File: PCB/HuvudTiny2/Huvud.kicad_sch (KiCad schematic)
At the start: 101 parts, among them J1 MOLEX Micro Fit 2x3, J2 DBG, J3 THERM, J4 FAN0, J5 FAN1, J6 Heater, J7 Endstop, J8 THERM, J9 STEPPER, Q1 AO3400A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

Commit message: Update screw terminal to molex connector.
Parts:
- J6: footprint Huvud:TerminalBlock_Phoenix_PT-1,5-2-3.5-H_1x02_P3.50mm_Horizontal -> Connector_Molex:Molex_Micro-Fit_3.0_43045-0200_2x01_P3.00mm_Horizontal
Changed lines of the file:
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@@
+    (pin "2")
+  )
+  (symbol (lib_id "Device:D") (at 194.945 109.22 0) (unit 1)
+    (in_bom yes) (on_board yes)
+    (property "Reference" "D4" (id 0) (at 191.77 108.3522 0))
+    (property "Value" "PMEG6010CEJ" (id 1) (at 194.945 105.5709 0))
+    (property "Footprint" "Diode_SMD:D_SOD-323F" (id 2) (at 194.945 109.22 0)
+      (effects (font (size 1.27 1.27)) hide)
+    )
+    (property "Datasheet" "~" (id 3) (at 194.945 109.22 0)
+      (effects (font (size 1.27 1.27)) hide)
+    )
+    (property "LCSC" "C406049" (id 4) (at 194.945 109.22 0)
+      (effects (font (size 1.27 1.27)) hide)
+    )
+    (pin "1")
     (pin "2")
   )
@@
     (pin "1")
   )
-  (symbol (lib_id "Device:D") (at 194.945 109.22 0) (unit 1)
-    (in_bom yes) (on_board yes)
-    (property "Reference" "D4" (id 0) (at 191.77 108.3522 0))
-    (property "Value" "PMEG6010CEJ" (id 1) (at 194.945 105.5709 0))
-    (property "Footprint" "Diode_SMD:D_SOD-323F" (id 2) (at 194.945 109.22 0)
-      (effects (font (size 1.27 1.27)) hide)
-    )
-    (property "Datasheet" "~" (id 3) (at 194.945 109.22 0)
-      (effects (font (size 1.27 1.27)) hide)
-    )
-    (property "LCSC" "C406049" (id 4) (at 194.945 109.22 0)
-      (effects (font (size 1.27 1.27)) hide)
-    )
-    (pin "1")
-    (pin "2")
-  )
   (symbol (lib_id "Mechanical:MountingHole_Pad") (at 249.555 118.745 0) (unit 1)
     (in_bom yes) (on_board yes)
@@
     (property "Reference" "J6" (id 0) (at 28.7528 168.91 0))
     (property "Value" "Heater" (id 1) (at 28.7528 170.4086 0))
-    (property "Footprint" "Huvud:TerminalBlock_Phoenix_PT-1,5-2-3.5-H_1x02_P3.50mm_Horizontal" (id 2) (at 29.21 172.72 0)
+    (property "Footprint" "Connector_Molex:Molex_Micro-Fit_3.0_43045-0200_2x01_P3.00mm_Horizontal" (id 2) (at 29.21 172.72 0)
       (effects (font (size 1.27 1.27)) hide)
     )
@@
     (pin "3")
     (pin "4")
+  )
+  (symbol (lib_id "Diode:BAT54S") (at 111.76 150.495 270) (mirror x) (unit 1)
+    (in_bom yes) (on_board yes)
+    (property "Reference" "D7" (id 0) (at 114.935 147.32 90))
+    (property "Value" "BAT54S" (id 1) (at 117.0686 145.415 90))
+    (property "Footprint" "Package_TO_SOT_SMD:SOT-23" (id 2) (at 114.935 148.59 0)
+      (effects (font (size 1.27 1.27)) (justify left) hide)
+    )
+    (property "Datasheet" "" (id 3) (at 111.76 153.543 0)
+      (effects (font (size 1.27 1.27)) hide)
+    )
+    (property "LCSC" "C12765" (id 4) (at 111.76 150.495 0)
+      (effects (font (size 1.27 1.27)) hide)
+    )
+    (pin "1")
+    (pin "2")
+    (pin "3")
+  )
+  (symbol (lib_id "Diode:BAT54S") (at 142.875 150.495 270) (mirror x) (unit 1)
+    (in_bom yes) (on_board yes)
+    (property "Reference" "D9" (id 0) (at 146.05 147.32 90))
+    (property "Value" "BAT54S" (id 1) (at 148.1836 145.415 90))
+    (property "Footprint" "Package_TO_SOT_SMD:SOT-23" (id 2) (at 146.05 148.59 0)
+      (effects (font (size 1.27 1.27)) (justify left) hide)
+    )
+    (property "Datasheet" "" (id 3) (at 142.875 153.543 0)
+      (effects (font (size 1.27 1.27)) hide)
+    )
+    (property "LCSC" "C12765" (id 4) (at 142.875 150.495 0)
+      (effects (font (size 1.27 1.27)) hide)
+    )
+    (pin "1")
+    (pin "2")
+    (pin "3")
+  )
+  (symbol (lib_id "Transistor_FET:2N7002") (at 50.8 121.92 0) (unit 1)
+    (in_bom yes) (on_board yes)
+    (property "Reference" "Q1" (id 0) (at 56.007 120.7516 0)
+      (effects (font (size 1.27 1.27)) (justify left))
+    )
+    (property "Value" "AO3400A" (id 1) (at 56.007 123.063 0)
+      (effects (font (size 1.27 1.27)) (justify left))
+    )
+    (property "Footprint" "Package_TO_SOT_SMD:SOT-23" (id 2) (at 55.88 123.825 0)
+      (effects (font (size 1.27 1.27) italic) (justify left) hide)
+    )
+    (property "Datasheet" "" (id 3) (at 50.8 121.92 0)
+      (effects (font (size 1.27 1.27)) (justify left) hide)
+    )
+    (property "LCSC" "C20917" (id 4) (at 50.8 121.92 0)
+      (effects (font (size 1.27 1.27)) hide)
+    )
+    (pin "1")
+    (pin "2")
+    (pin "3")
+  )
+  (symbol (lib_id "Transistor_FET:2N7002") (at 52.07 151.13 0) (unit 1)
+    (in_bom yes) (on_board yes)
+    (property "Reference" "Q2" (id 0) (at 57.277 149.9616 0)
+      (effects (font (size 1.27 1.27)) (justify left))
+    )
+    (property "Value" "AO3400A" (id 1) (at 57.277 152.273 0)
+      (effects (font (size 1.27 1.27)) (justify left))
+    )
+    (property "Footprint" "Package_TO_SOT_SMD:SOT-23" (id 2) (at 57.15 153.035 0)
+      (effects (font (size 1.27 1.27) italic) (justify left) hide)
+    )
+    (property "Datasheet" "" (id 3) (at 52.07 151.13 0)
+      (effects (font (size 1.27 1.27)) (justify left) hide)
+    )
+    (property "LCSC" "C20917" (id 4) (at 52.07 151.13 0)
+      (effects (font (size 1.27 1.27)) hide)
+    )
+    (pin "1")
+    (pin "2")
+    (pin "3")
+  )
+  (symbol (lib_id "Huvud:AON7418") (at 54.61 167.64 0) (unit 1)
+    (in_bom yes) (on_board yes)
+    (property "Reference" "Q3" (id 0) (at 57.15 179.07 0)
+      (effects (font (size 1.27 1.27)) (justify left))
+    )
+    (property "Value" "AON7534" (id 1) (at 57.15 181.61 0)
+      (effects (font (size 1.27 1.27)) (justify left))
+    )
+    (property "Footprint" "Huvud:DFN-8-1EP_3x3mm_P0.65mm_EP1.7x2.05mm" (id 2) (at 59.69 169.545 0)
+      (effects (font (size 1.27 1.27) italic) (justify left) hide)
+    )
+    (property "Datasheet" "" (id 3) (at 54.61 167.64 0)
+      (effects (font (size 1.27 1.27)) (justify left) hide)
+    )
+    (property "LCSC" "C115844" (id 4) (at 54.61 167.64 0)
+      (effects (font (size 1.27 1.27)) hide)
+    )
+    (pin "1")
+    (pin "2")
+    (pin "3")
   )
   (symbol (lib_id "Connector_Generic:Conn_02x03_Odd_Even") (at 133.35 115.57 180) (unit 1)
@@
     (pin "5")
     (pin "6")
-  )
-  (symbol (lib_id "Diode:BAT54S") (at 111.76 150.495 270) (mirror x) (unit 1)
-    (in_bom yes) (on_board yes)
-    (property "Reference" "D7" (id 0) (at 114.935 147.32 90))
-    (property "Value" "BAT54S" (id 1) (at 117.0686 145.415 90))
-    (property "Footprint" "Package_TO_SOT_SMD:SOT-23" (id 2) (at 114.935 148.59 0)
-      (effects (font (size 1.27 1.27)) (justify left) hide)
-    )
-    (property "Datasheet" "" (id 3) (at 111.76 153.543 0)
-      (effects (font (size 1.27 1.27)) hide)
-    )
-    (property "LCSC" "C12765" (id 4) (at 111.76 150.495 0)
-      (effects (font (size 1.27 1.27)) hide)
-    )
-    (pin "1")
-    (pin "2")
-    (pin "3")
-  )
-  (symbol (lib_id "Diode:BAT54S") (at 142.875 150.495 270) (mirror x) (unit 1)
-    (in_bom yes) (on_board yes)
-    (property "Reference" "D9" (id 0) (at 146.05 147.32 90))
-    (property "Value" "BAT54S" (id 1) (at 148.1836 145.415 90))
-    (property "Footprint" "Package_TO_SOT_SMD:SOT-23" (id 2) (at 146.05 148.59 0)
-      (effects (font (size 1.27 1.27)) (justify left) hide)
-    )
-    (property "Datasheet" "" (id 3) (at 142.875 153.543 0)
-      (effects (font (size 1.27 1.27)) hide)
-    )
-    (property "LCSC" "C12765" (id 4) (at 142.875 150.495 0)
-      (effects (font (size 1.27 1.27)) hide)
-    )
-    (pin "1")
-    (pin "2")
-    (pin "3")
-  )
-  (symbol (lib_id "Transistor_FET:2N7002") (at 50.8 121.92 0) (unit 1)
-    (in_bom yes) (on_board yes)
-    (property "Reference" "Q1" (id 0) (at 56.007 120.7516 0)
-      (effects (font (size 1.27 1.27)) (justify left))
-    )
-    (property "Value" "AO3400A" (id 1) (at 56.007 123.063 0)
-      (effects (font (size 1.27 1.27)) (justify left))
-    )
-    (property "Footprint" "Package_TO_SOT_SMD:SOT-23" (id 2) (at 55.88 123.825 0)
-      (effects (font (size 1.27 1.27) italic) (justify left) hide)
-    )
-    (property "Datasheet" "" (id 3) (at 50.8 121.92 0)
-      (effects (font (size 1.27 1.27)) (justify left) hide)
-    )
-    (property "LCSC" "C20917" (id 4) (at 50.8 121.92 0)
-      (effects (font (size 1.27 1.27)) hide)
-    )
-    (pin "1")
-    (pin "2")
-    (pin "3")
-  )
-  (symbol (lib_id "Transistor_FET:2N7002") (at 52.07 151.13 0) (unit 1)
-    (in_bom yes) (on_board yes)
-    (property "Reference" "Q2" (id 0) (at 57.277 149.9616 0)
-      (effects (font (size 1.27 1.27)) (justify left))
-    )
-    (property "Value" "AO3400A" (id 1) (at 57.277 152.273 0)
-      (effects (font (size 1.27 1.27)) (justify left))
-    )
-    (property "Footprint" "Package_TO_SOT_SMD:SOT-23" (id 2) (at 57.15 153.035 0)
-      (effects (font (size 1.27 1.27) italic) (justify left) hide)
-    )
-    (property "Datasheet" "" (id 3) (at 52.07 151.13 0)
-      (effects (font (size 1.27 1.27)) (justify left) hide)
-    )
-    (property "LCSC" "C20917" (id 4) (at 52.07 151.13 0)
-      (effects (font (size 1.27 1.27)) hide)
-    )
-    (pin "1")
-    (pin "2")
-    (pin "3")
-  )
-  (symbol (lib_id "Huvud:AON7418") (at 54.61 167.64 0) (unit 1)
-    (in_bom yes) (on_board yes)
-    (property "Reference" "Q3" (id 0) (at 57.15 179.07 0)
-      (effects (font (size 1.27 1.27)) (justify left))
-    )
-    (property "Value" "AON7534" (id 1) (at 57.15 181.61 0)
-      (effects (font (size 1.27 1.27)) (justify left))
-    )
-    (property "Footprint" "Huvud:DFN-8-1EP_3x3mm_P0.65mm_EP1.7x2.05mm" (id 2) (at 59.69 169.545 0)
-      (effects (font (size 1.27 1.27) italic) (justify left) hide)
-    )
-    (property "Datasheet" "" (id 3) (at 54.61 167.64 0)
-      (effects (font (size 1.27 1.27)) (justify left) hide)
-    )
-    (property "LCSC" "C115844" (id 4) (at 54.61 167.64 0)
-      (effects (font (size 1.27 1.27)) hide)
-    )
-    (pin "1")
-    (pin "2")
-    (pin "3")
   )
   (symbol (lib_id "Graphic:Logo_Open_Hardware_Small") (at 161.925 189.23 0) (unit 1)
@@
     )
     (path "/00000000-0000-0000-0000-00005e7a5abd"
-      (reference "J6") (unit 1) (value "Heater") (footprint "Huvud:TerminalBlock_Phoenix_PT-1,5-2-3.5-H_1x02_P3.50mm_Horizontal")
+      (reference "J6") (unit 1) (value "Heater") (footprint "Connector_Molex:Molex_Micro-Fit_3.0_43045-0200_2x01_P3.00mm_Horizontal")
     )
     (path "/00000000-0000-0000-0000-00005eee4c5c"

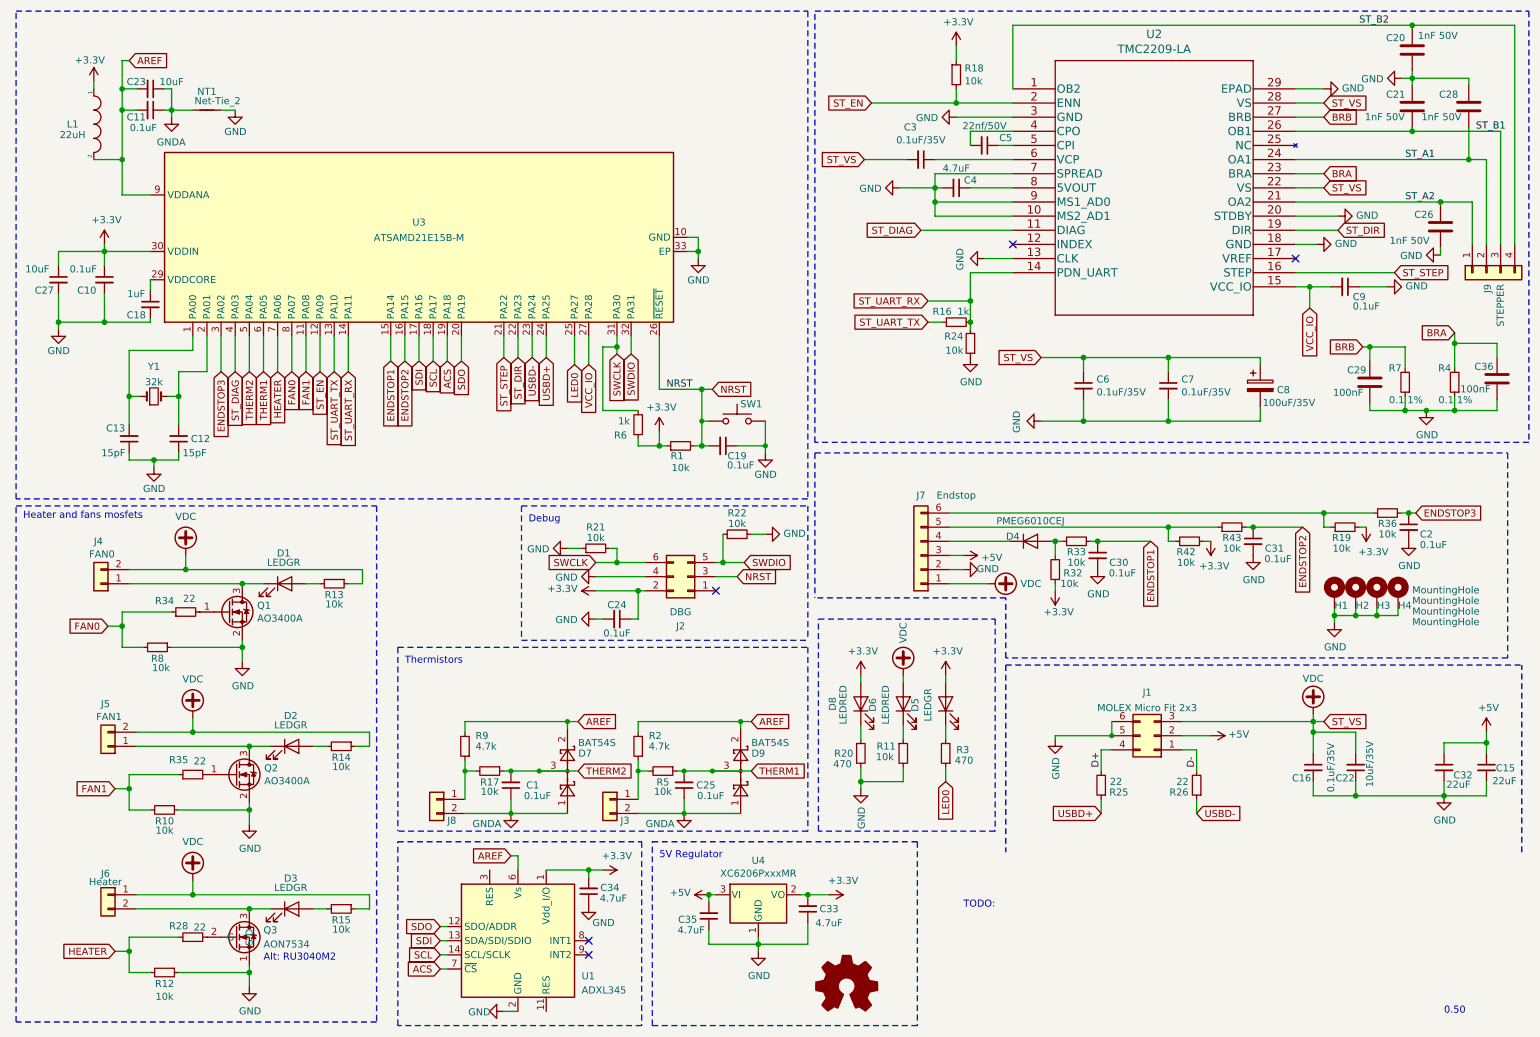
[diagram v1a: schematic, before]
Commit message: Add third fan mosfet (could be used for lighing).
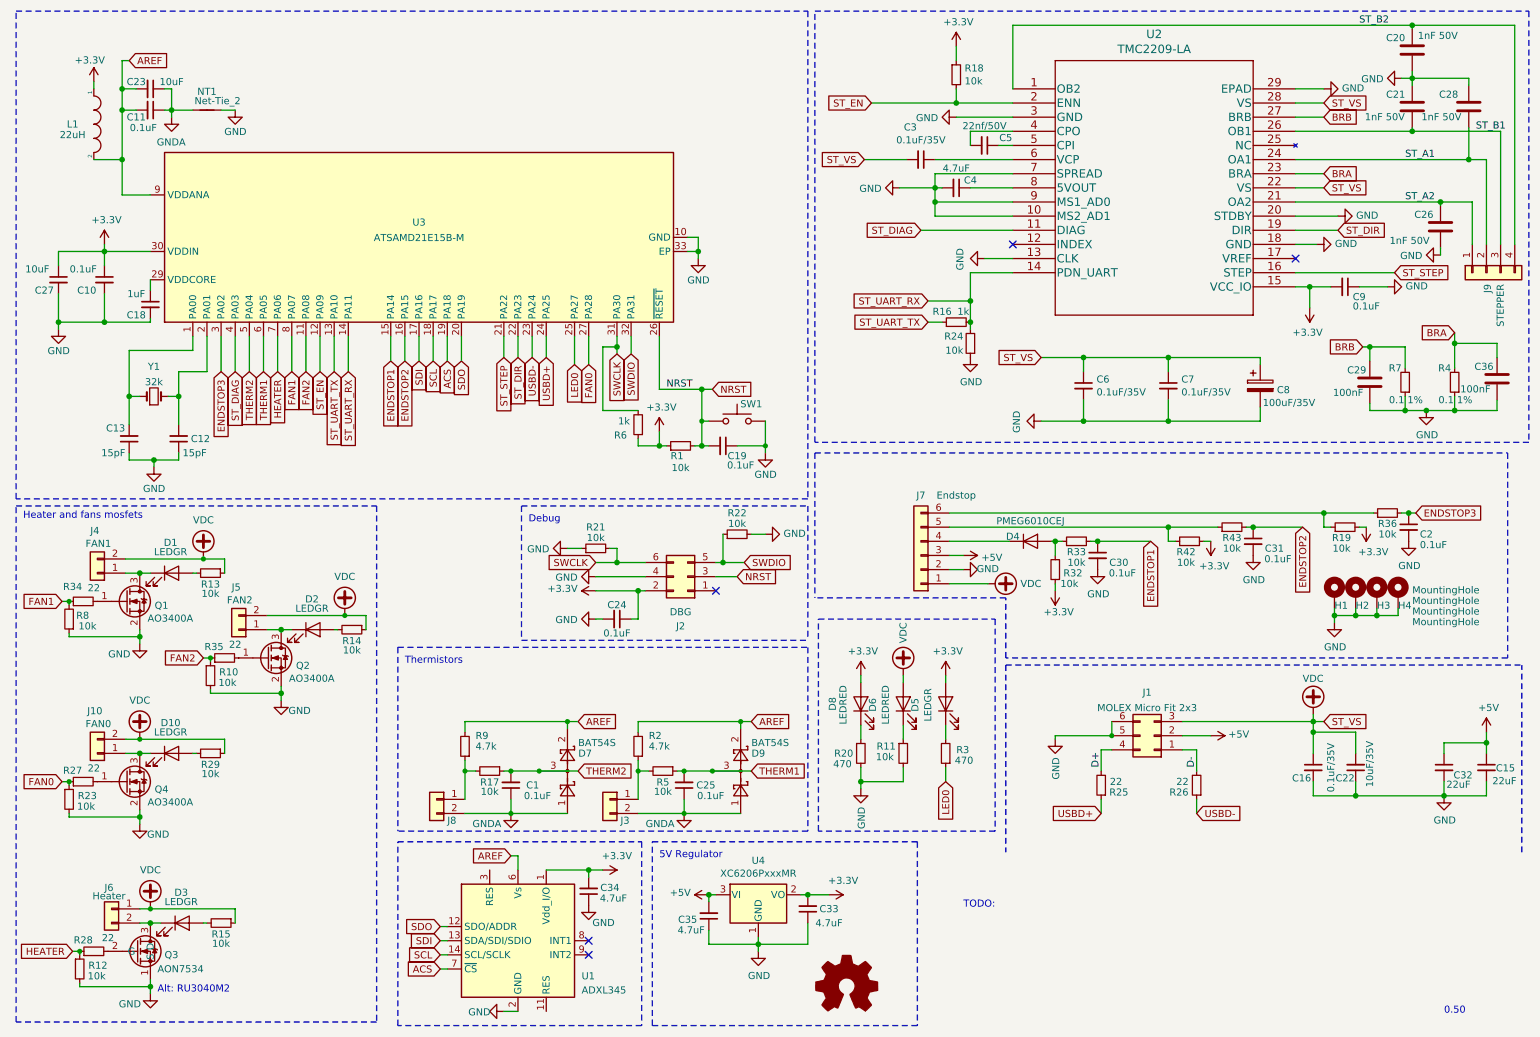
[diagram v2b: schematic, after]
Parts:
- added D10: LEDGR, LED_SMD:LED_0402_1005Metric, symbol Device:LED
- added J10: FAN0, Connector_Hirose:Hirose_DF13-02P-1.25DSA_1x02_P1.25mm_Vertical, symbol Connector_Generic:Conn_01x02
- added Q4: AO3400A, Package_TO_SOT_SMD:SOT-23, symbol Transistor_FET:2N7002
- added R23, R29: 10k, Resistor_SMD:R_0402_1005Metric, symbol Device:R_Small
- added R27: 22, Resistor_SMD:R_0402_1005Metric, symbol Device:R_Small
- J4: value FAN0 -> FAN1
- J5: value FAN1 -> FAN2
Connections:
- net +3V3: now also C9.2, U2.15 (VCC_IO)
- net FAN0: now also U3.27 (PA28), R23.1, R27.1; no longer R34.1, R8.2, U3.8 (PA07)
- net FAN1: now also R34.1, R8.2, U3.8 (PA07); no longer R10.2, R35.1, U3.11 (PA08)
- net GND: now also R10.2, R12.2, Q4.2 (S), R23.2; no longer R10.1, R12.1
- net HEATER: now also R12.1; no longer R12.2
- net VDC: now also J10.2 (Pin_2), R29.1
- removed net VCC_IO: C9.2, U2.15 (VCC_IO), U3.27 (PA28)
- new net: D10.1 (K), J10.1 (Pin_1), Q4.3 (D)
- new net: D10.2 (A), R29.2
- new net: Q4.1 (G), R27.2
- new net FAN2: R10.1, R35.1, U3.11 (PA08)
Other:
- moved on the sheet: D1, D2, D3, J4, J5, J6, Q1, Q2, Q3, R10, R12, R13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

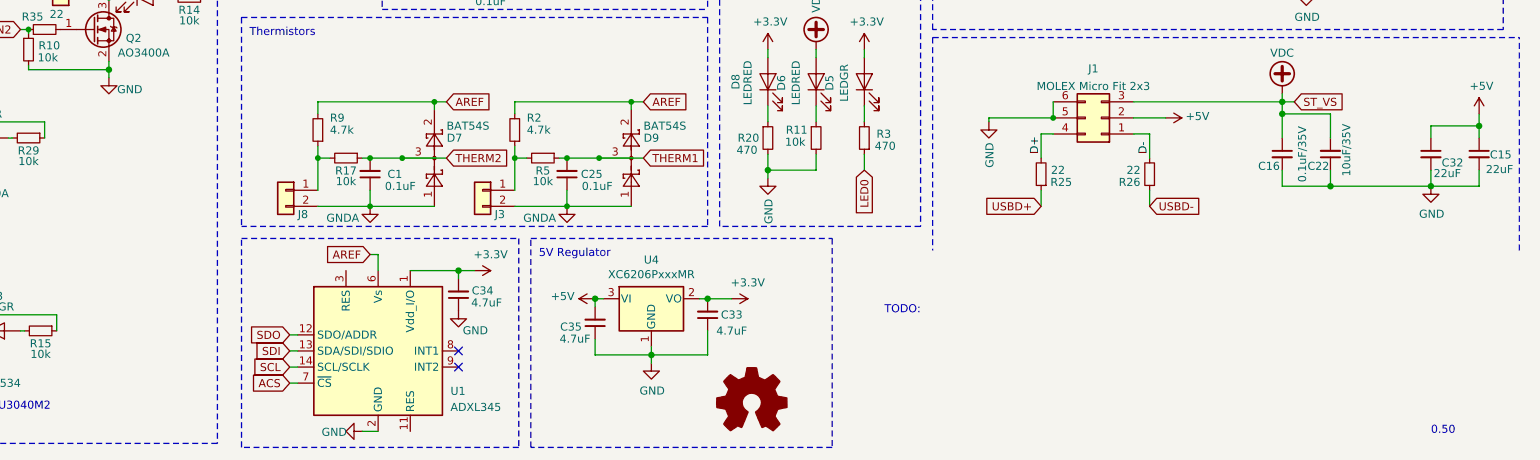
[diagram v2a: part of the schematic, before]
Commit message: LDO power supply from 24V.
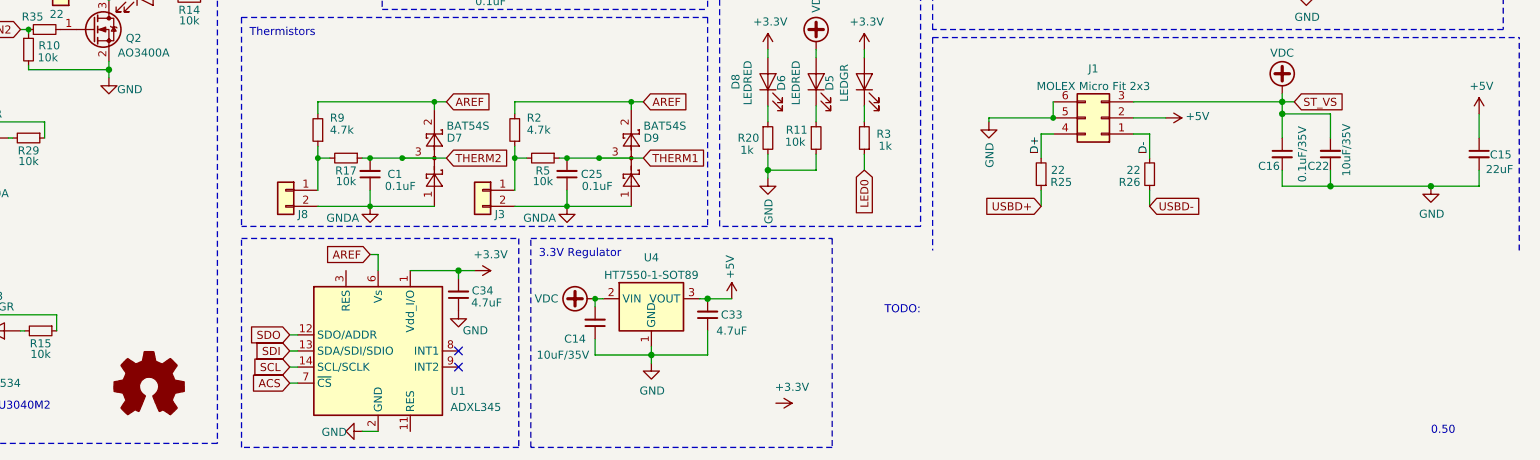
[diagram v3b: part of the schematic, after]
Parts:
- removed C32: 22uF, Capacitor_SMD:C_0805_2012Metric, symbol Device:C_Small
- removed C35: 4.7uF, Capacitor_SMD:C_0402_1005Metric, symbol Device:C_Small
- removed U4: XC6206PxxxMR, Package_TO_SOT_SMD:SOT-23, symbol Regulator_Linear:XC6206PxxxMR
- added C14: 10uF/35V, Capacitor_SMD:C_1206_3216Metric, symbol Device:C_Small
- added U4: HT7550-1-SOT89, Package_TO_SOT_SMD:SOT-89-3, symbol Regulator_Linear:HT75xx-1-SOT89
- R20, R3: value 470 -> 1k; LCSC C25117 -> C11702
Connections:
- net +3V3: no longer C33.2
- net +5V: now also C33.2, U4.3 (VOUT)
- net GND: now also C14.1, U4.1 (GND)
- net VDC: now also C14.2, U4.2 (VIN)
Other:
- note added: "3.3V Regulator"
- note removed: "5V Regulator"
